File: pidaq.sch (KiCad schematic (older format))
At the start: 42 parts, among them J1 Screw_Terminal_01x08, J2 Screw_Terminal_01x08, J3 Screw_Terminal_01x10, J4 Screw_Terminal_01x10, J5 Conn_01x03_Male, J6 Conn_01x08_Female, U1 LTC2984CLX-DNP, U2 LTC2418IGN-DNP, U3 SN74LV1T34DCKR

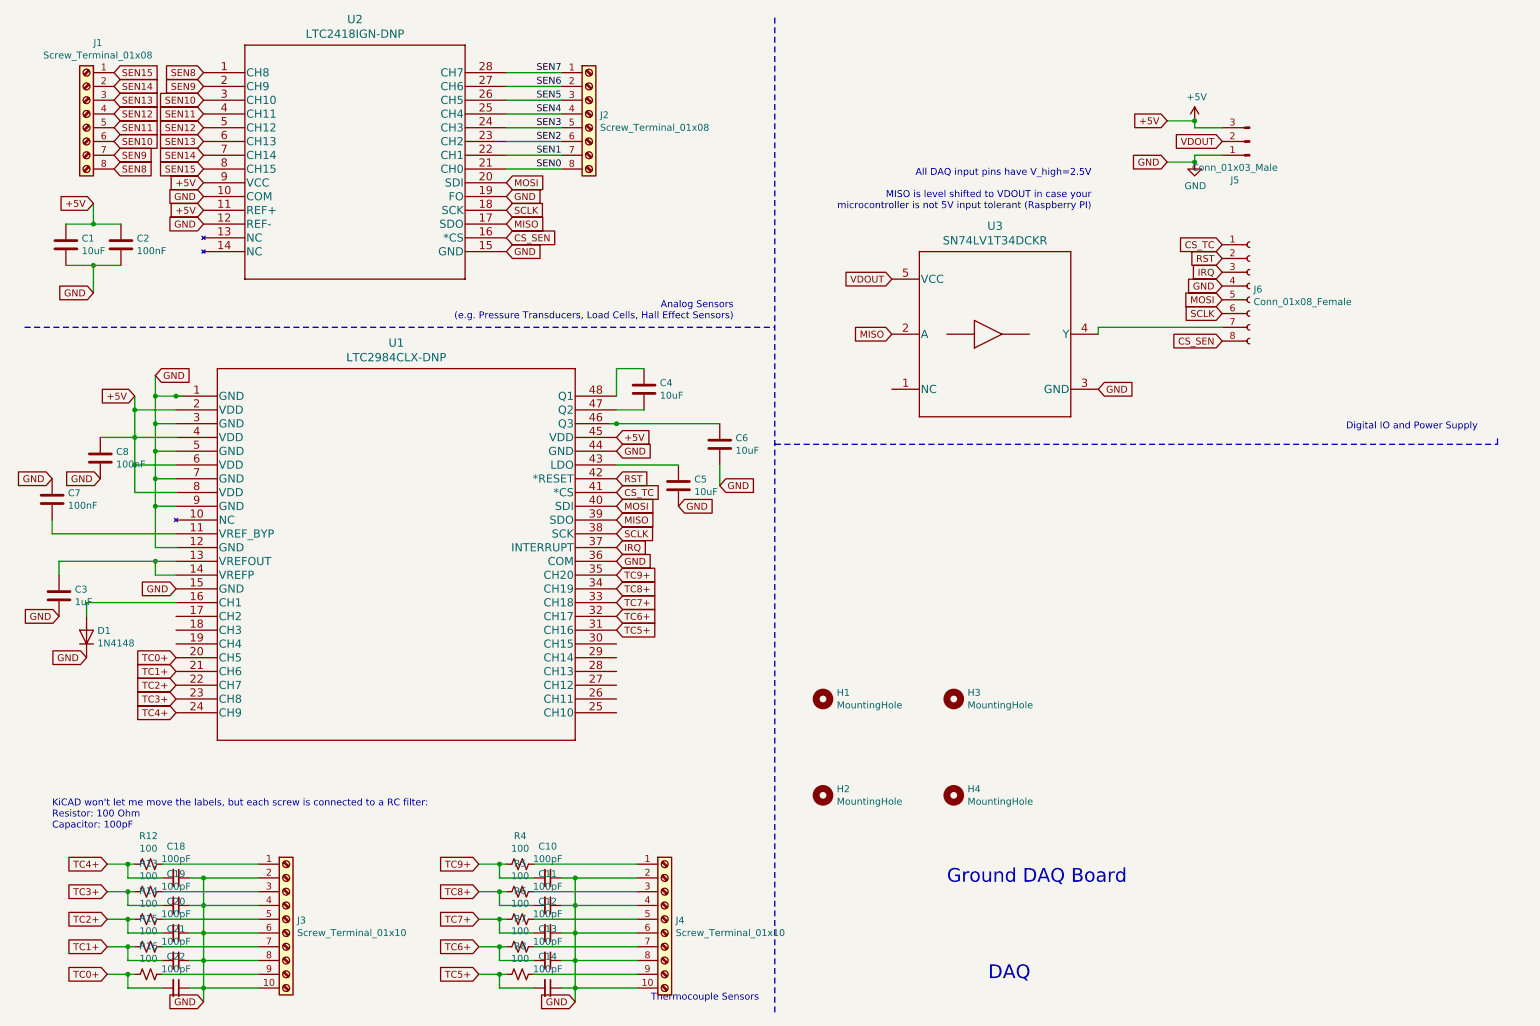
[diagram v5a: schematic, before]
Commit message: reversed screw terminal symbols
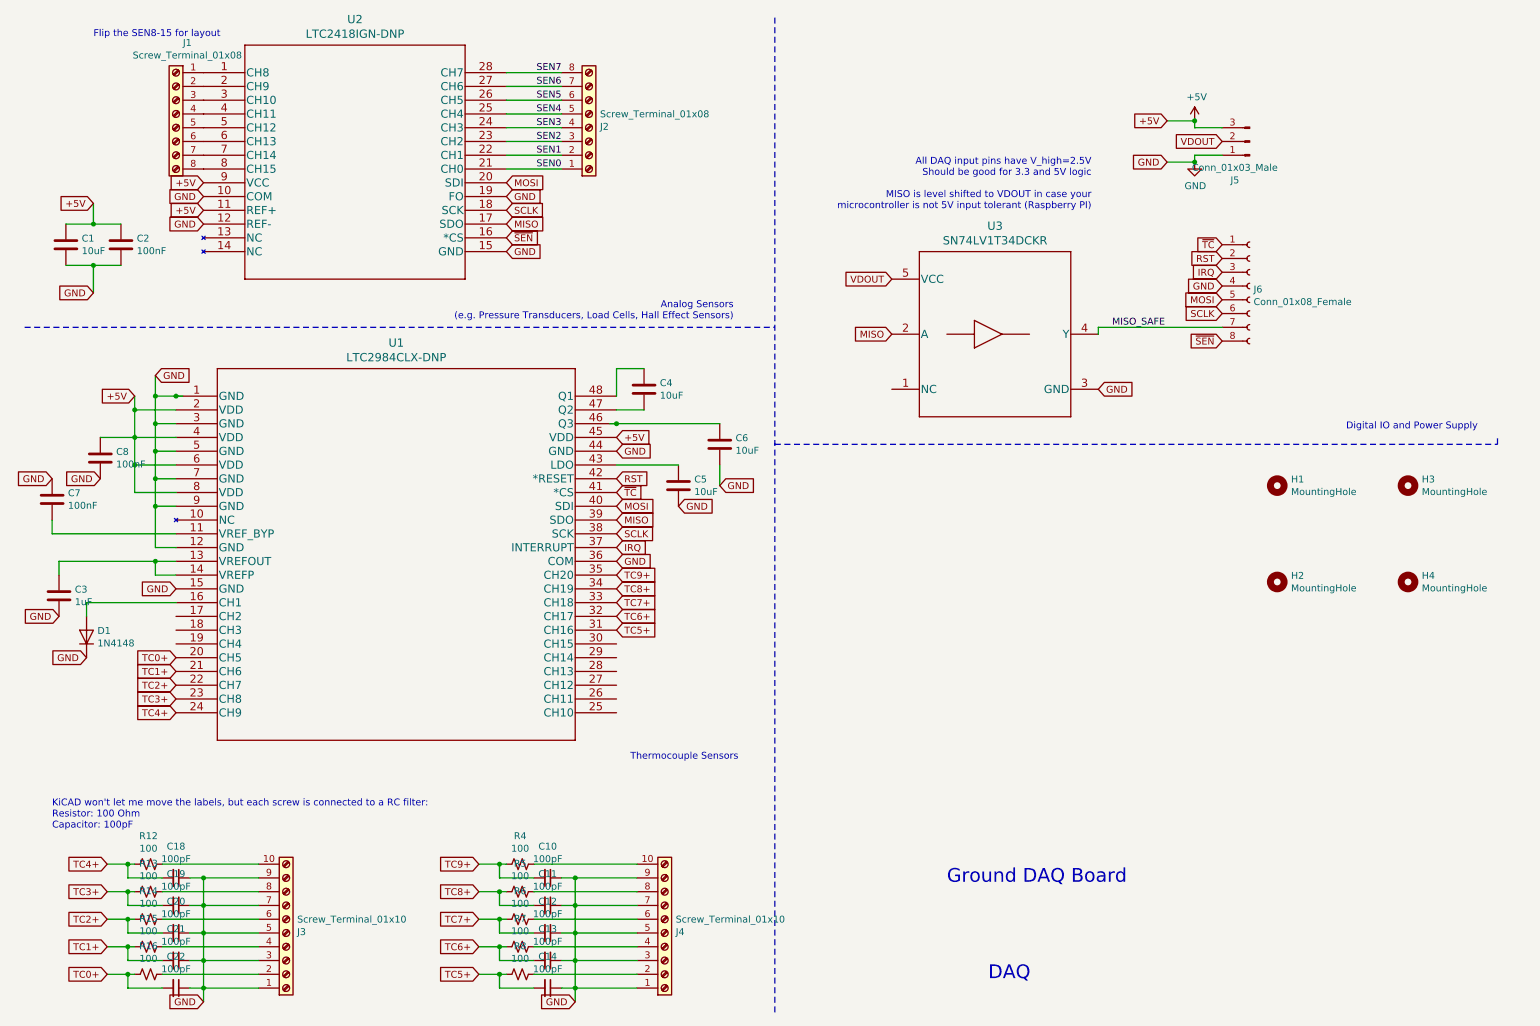
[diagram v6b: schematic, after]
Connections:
- net GND: now also J3.1 (Pin_1), J3.3 (Pin_3), J3.5 (Pin_5), J3.7 (Pin_7), J3.9 (Pin_9), J4.1 (Pin_1), J4.3 (Pin_3), J4.5 (Pin_5), J4.7 (Pin_7), J4.9 (Pin_9); no longer J3.10 (Pin_10), J3.2 (Pin_2), J3.4 (Pin_4), J3.6 (Pin_6), J3.8 (Pin_8), J4.10 (Pin_10), J4.2 (Pin_2), J4.4 (Pin_4), J4.6 (Pin_6), J4.8 (Pin_8)
- net SEN0: now also J2.1 (Pin_1); no longer J2.8 (Pin_8)
- net SEN1: now also J2.2 (Pin_2); no longer J2.7 (Pin_7)
- net SEN2: now also J2.3 (Pin_3); no longer J2.6 (Pin_6)
- net SEN3: now also J2.4 (Pin_4); no longer J2.5 (Pin_5)
- net SEN4: now also J2.5 (Pin_5); no longer J2.4 (Pin_4)
- net SEN5: now also J2.6 (Pin_6); no longer J2.3 (Pin_3)
- net SEN6: now also J2.7 (Pin_7); no longer J2.2 (Pin_2)
- net SEN7: now also J2.8 (Pin_8); no longer J2.1 (Pin_1)
- net MISO_SAFE: now reaches J6.7 (Pin_7), U3.4 (Y)
- net at R4.1: now also J4.10 (Pin_10); no longer J4.1 (Pin_1)
- net at R5.1: now also J4.8 (Pin_8); no longer J4.3 (Pin_3)
- net at R6.1: now also J4.6 (Pin_6); no longer J4.5 (Pin_5)
- net at R7.1: now also J4.4 (Pin_4); no longer J4.7 (Pin_7)
- net at R8.1: now also J4.2 (Pin_2); no longer J4.9 (Pin_9)
- net at R16.1: now also J3.2 (Pin_2); no longer J3.9 (Pin_9)
- net at R15.1: now also J3.4 (Pin_4); no longer J3.7 (Pin_7)
- net at R14.1: now also J3.6 (Pin_6); no longer J3.5 (Pin_5)
- net at R13.1: now also J3.8 (Pin_8); no longer J3.3 (Pin_3)
- net at R12.1: now also J3.10 (Pin_10); no longer J3.1 (Pin_1)
- net CS_SEN renamed ~SEN
- net CS_TC renamed ~TC
- net SEN10: no longer names the net of U2.3 (CH10)
- net SEN10: now also J1.3 (Pin_3); no longer J1.6 (Pin_6)
- net SEN11: no longer names the net of U2.4 (CH11)
- net SEN11: now also J1.4 (Pin_4); no longer J1.5 (Pin_5)
- net SEN12: no longer names the net of U2.5 (CH12)
- net SEN12: now also J1.5 (Pin_5); no longer J1.4 (Pin_4)
- net SEN13: no longer names the net of U2.6 (CH13)
- net SEN13: now also J1.6 (Pin_6); no longer J1.3 (Pin_3)
- net SEN14: no longer names the net of J1.2 (Pin_2)
- net SEN14: now also U2.2 (CH9); no longer U2.7 (CH14)
- net SEN15: no longer names the net of J1.1 (Pin_1)
- net SEN15: now also U2.1 (CH8); no longer U2.8 (CH15)
- net SEN8: no longer names the net of J1.8 (Pin_8)
- net SEN8: now also U2.8 (CH15); no longer U2.1 (CH8)
- net SEN9: no longer names the net of J1.7 (Pin_7)
- net SEN9: now also U2.7 (CH14); no longer U2.2 (CH9)
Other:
- note added: "All DAQ input pins have V_high=2.5V\nShould be good for 3.3 and 5V logic\n\nMISO is level shifted to VDOUT in case your\nmicrocontroller is not 5V input tolerant (Raspberry PI)"
- note added: "Flip the SEN8-15 for layout"
- note removed: "All DAQ input pins have V_high=2.5V\n\nMISO is level shifted to VDOUT in case your\nmicrocontroller is not 5V input tolerant (Raspberry PI)"
- moved on the sheet: H1, H2, H3, H4, J1
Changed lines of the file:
@@
 L Connector:Screw_Terminal_01x08 J2
 U 1 1 5EDBB95D
-P 4550 1250
+P 4550 1350
 AR Path="/5EDBB95D" Ref="J2"  Part="1"
 AR Path="/5ED56214/5EDBB95D" Ref="J?"  Part="1"
-F 0 "J2" H 4630 1242 50  0000 L CNN
-F 1 "Screw_Terminal_01x08" H 4630 1151 50  0000 L CNN
-F 2 "TerminalBlock_Phoenix:TerminalBlock_Phoenix_MKDS-1,5-8-5.08_1x08_P5.08mm_Horizontal" H 4550 1250 50  0001 C CNN
-F 3 "~" H 4550 1250 50  0001 C CNN
-	1    4550 1250
-	1    0    0    -1
+F 0 "J2" H 4630 1342 50  0000 L CNN
+F 1 "Screw_Terminal_01x08" H 4630 1251 50  0000 L CNN
+F 2 "TerminalBlock_Phoenix:TerminalBlock_Phoenix_MKDS-1,5-8-5.08_1x08_P5.08mm_Horizontal" H 4550 1350 50  0001 C CNN
+F 3 "~" H 4550 1350 50  0001 C CNN
+	1    4550 1350
+	1    0    0    1
 $EndComp
 $Comp
 L Connector:Screw_Terminal_01x08 J1
 U 1 1 5EDBB963
-P 900 1250
+P 1550 1250
 AR Path="/5EDBB963" Ref="J1"  Part="1"
 AR Path="/5ED56214/5EDBB963" Ref="J?"  Part="1"
-F 0 "J1" H 818 1767 50  0000 C CNN
-F 1 "Screw_Terminal_01x08" H 818 1676 50  0000 C CNN
-F 2 "TerminalBlock_Phoenix:TerminalBlock_Phoenix_MKDS-1,5-8-5.08_1x08_P5.08mm_Horizontal" H 900 1250 50  0001 C CNN
-F 3 "~" H 900 1250 50  0001 C CNN
-	1    900  1250
+F 0 "J1" H 1468 1767 50  0000 C CNN
+F 1 "Screw_Terminal_01x08" H 1468 1676 50  0000 C CNN
+F 2 "TerminalBlock_Phoenix:TerminalBlock_Phoenix_MKDS-1,5-8-5.08_1x08_P5.08mm_Horizontal" H 1550 1250 50  0001 C CNN
+F 3 "~" H 1550 1250 50  0001 C CNN
+	1    1550 1250
 	-1   0    0    -1
 $EndComp
@@
 SCLK
 Text GLabel 3950 2150 2    50   Input ~ 0
-CS_SEN
+~SEN
 Text Notes 5600 2750 2    50   ~ 0
 Analog Sensors \n(e.g. Pressure Transducers, Load Cells, Hall Effect Sensors)
@@
 RST
 Text GLabel 4750 4000 2    50   Input ~ 0
-CS_TC
+~TC
 Text GLabel 4750 4100 2    50   Input ~ 0
 MOSI
@@
 Wire Wire Line
 	3900 7500 3750 7500
-Text GLabel 1750 950  0    50   Input ~ 0
-SEN8
-Text GLabel 1750 1050 0    50   Input ~ 0
-SEN9
-Text GLabel 1750 1150 0    50   Input ~ 0
-SEN10
-Text GLabel 1750 1250 0    50   Input ~ 0
-SEN11
-Text GLabel 1750 1350 0    50   Input ~ 0
-SEN12
-Text GLabel 1750 1450 0    50   Input ~ 0
-SEN13
-Text GLabel 1750 1550 0    50   Input ~ 0
-SEN14
-Text GLabel 1750 1650 0    50   Input ~ 0
-SEN15
-Text GLabel 1100 950  2    50   Input ~ 0
-SEN15
-Text GLabel 1100 1050 2    50   Input ~ 0
-SEN14
-Text GLabel 1100 1150 2    50   Input ~ 0
-SEN13
-Text GLabel 1100 1250 2    50   Input ~ 0
-SEN12
-Text GLabel 1100 1350 2    50   Input ~ 0
-SEN11
-Text GLabel 1100 1450 2    50   Input ~ 0
-SEN10
-Text GLabel 1100 1550 2    50   Input ~ 0
-SEN9
-Text GLabel 1100 1650 2    50   Input ~ 0
-SEN8
 Text GLabel 4750 4700 2    50   Input ~ 0
 TC8+
@@
 Text GLabel 3750 7100 0    50   Input ~ 0
 TC7+
-Text Notes 5000 7700 0    50   ~ 0
+Text Notes 4850 5950 0    50   ~ 0
 Thermocouple Sensors\n
 $Comp
@@
 $EndComp
 Text GLabel 9150 2900 0    50   Input ~ 0
-CS_SEN
-Text GLabel 9150 2200 0    50   Input ~ 0
-CS_TC
+~SEN
 Text GLabel 9150 2300 0    50   Input ~ 0
 RST
@@
 L Connector:Screw_Terminal_01x10 J3
 U 1 1 5F0EBDBF
-P 2350 7100
-F 0 "J3" H 2430 7092 50  0000 L CNN
-F 1 "Screw_Terminal_01x10" H 2430 7001 50  0000 L CNN
-F 2 "TerminalBlock_Phoenix:TerminalBlock_Phoenix_PT-1,5-10-3.5-H_1x10_P3.50mm_Horizontal" H 2350 7100 50  0001 C CNN
-F 3 "~" H 2350 7100 50  0001 C CNN
-	1    2350 7100
-	1    0    0    -1
-$EndComp
-$Comp
-L Connector:Screw_Terminal_01x10 J4
-U 1 1 5F0EED09
-P 5100 7100
-F 0 "J4" H 5180 7092 50  0000 L CNN
-F 1 "Screw_Terminal_01x10" H 5180 7001 50  0000 L CNN
-F 2 "TerminalBlock_Phoenix:TerminalBlock_Phoenix_PT-1,5-10-3.5-H_1x10_P3.50mm_Horizontal" H 5100 7100 50  0001 C CNN
-F 3 "~" H 5100 7100 50  0001 C CNN
-	1    5100 7100
-	1    0    0    -1
+P 2350 7200
+F 0 "J3" H 2430 7192 50  0000 L CNN
+F 1 "Screw_Terminal_01x10" H 2430 7101 50  0000 L CNN
+F 2 "TerminalBlock_Phoenix:TerminalBlock_Phoenix_PT-1,5-10-3.5-H_1x10_P3.50mm_Horizontal" H 2350 7200 50  0001 C CNN
+F 3 "~" H 2350 7200 50  0001 C CNN
+	1    2350 7200
+	1    0    0    1
 $EndComp
 Wire Wire Line
@@
 	1450 6700 2150 6700
 Wire Wire Line
-	4150 6700 4900 6700
-Wire Wire Line
-	4450 6800 4900 6800
-Wire Wire Line
-	4150 6900 4900 6900
-Wire Wire Line
 	4350 7000 4450 7000
-Wire Wire Line
-	4450 7000 4900 7000
-Wire Wire Line
-	4150 7100 4900 7100
-Wire Wire Line
-	4450 7200 4900 7200
-Wire Wire Line
-	4150 7300 4900 7300
-Wire Wire Line
-	4450 7400 4900 7400
-Wire Wire Line
-	4150 7500 4900 7500
-Wire Wire Line
-	4450 7600 4900 7600
 $Comp
 L Diode:1N4148 D1
@@
 L Mechanical:MountingHole H1
 U 1 1 5ED3CDC2
-P 6250 5500
-F 0 "H1" H 6350 5546 50  0000 L CNN
-F 1 "MountingHole" H 6350 5455 50  0000 L CNN
-F 2 "MountingHole:MountingHole_3.2mm_M3" H 6250 5500 50  0001 C CNN
-F 3 "~" H 6250 5500 50  0001 C CNN
-	1    6250 5500
+P 9550 3950
+F 0 "H1" H 9650 3996 50  0000 L CNN
+F 1 "MountingHole" H 9650 3905 50  0000 L CNN
+F 2 "MountingHole:MountingHole_3.2mm_M3" H 9550 3950 50  0001 C CNN
+F 3 "~" H 9550 3950 50  0001 C CNN
+	1    9550 3950
 	1    0    0    -1
 $EndComp
@@
 L Mechanical:MountingHole H3
 U 1 1 5ED3DEFD
-P 7200 5500
-F 0 "H3" H 7300 5546 50  0000 L CNN
-F 1 "MountingHole" H 7300 5455 50  0000 L CNN
-F 2 "MountingHole:MountingHole_3.2mm_M3" H 7200 5500 50  0001 C CNN
-F 3 "~" H 7200 5500 50  0001 C CNN
-	1    7200 5500
+P 10500 3950
+F 0 "H3" H 10600 3996 50  0000 L CNN
+F 1 "MountingHole" H 10600 3905 50  0000 L CNN
+F 2 "MountingHole:MountingHole_3.2mm_M3" H 10500 3950 50  0001 C CNN
+F 3 "~" H 10500 3950 50  0001 C CNN
+	1    10500 3950
 	1    0    0    -1
 $EndComp
@@
 L Mechanical:MountingHole H2
 U 1 1 5ED3EC92
-P 6250 6200
-F 0 "H2" H 6350 6246 50  0000 L CNN
-F 1 "MountingHole" H 6350 6155 50  0000 L CNN
-F 2 "MountingHole:MountingHole_3.2mm_M3" H 6250 6200 50  0001 C CNN
-F 3 "~" H 6250 6200 50  0001 C CNN
-	1    6250 6200
+P 9550 4650
+F 0 "H2" H 9650 4696 50  0000 L CNN
+F 1 "MountingHole" H 9650 4605 50  0000 L CNN
+F 2 "MountingHole:MountingHole_3.2mm_M3" H 9550 4650 50  0001 C CNN
+F 3 "~" H 9550 4650 50  0001 C CNN
+	1    9550 4650
 	1    0    0    -1
 $EndComp
@@
 L Mechanical:MountingHole H4
 U 1 1 5ED3F653
-P 7200 6200
-F 0 "H4" H 7300 6246 50  0000 L CNN
-F 1 "MountingHole" H 7300 6155 50  0000 L CNN
-F 2 "MountingHole:MountingHole_3.2mm_M3" H 7200 6200 50  0001 C CNN
-F 3 "~" H 7200 6200 50  0001 C CNN
-	1    7200 6200
+P 10500 4650
+F 0 "H4" H 10600 4696 50  0000 L CNN
+F 1 "MountingHole" H 10600 4605 50  0000 L CNN
+F 2 "MountingHole:MountingHole_3.2mm_M3" H 10500 4650 50  0001 C CNN
+F 3 "~" H 10500 4650 50  0001 C CNN
+	1    10500 4650
 	1    0    0    -1
 $EndComp
@@
 Digital IO and Power Supply
 Text Notes 8200 1950 2    50   ~ 0
-All DAQ input pins have V_high=2.5V\n\nMISO is level shifted to VDOUT in case your\nmicrocontroller is not 5V input tolerant (Raspberry PI)
+All DAQ input pins have V_high=2.5V\nShould be good for 3.3 and 5V logic\n\nMISO is level shifted to VDOUT in case your\nmicrocontroller is not 5V input tolerant (Raspberry PI)
+Text Label 8350 2800 0    50   ~ 0
+MISO_SAFE
+Text Notes 950  700  0    50   ~ 0
+Flip the SEN8-15 for layout
+Text GLabel 9150 2200 0    50   Input ~ 0
+~TC
+Wire Wire Line
+	4450 7600 4900 7600
+Wire Wire Line
+	4150 7500 4900 7500
+Wire Wire Line
+	4450 7400 4900 7400
+Wire Wire Line
+	4150 7300 4900 7300
+Wire Wire Line
+	4450 7200 4900 7200
+Wire Wire Line
+	4150 7100 4900 7100
+Wire Wire Line
+	4450 7000 4900 7000
+Wire Wire Line
+	4150 6900 4900 6900
+Wire Wire Line
+	4450 6800 4900 6800
+Wire Wire Line
+	4150 6700 4900 6700
+$Comp
+L Connector:Screw_Terminal_01x10 J4
+U 1 1 5F0EED09
+P 5100 7200
+F 0 "J4" H 5180 7192 50  0000 L CNN
+F 1 "Screw_Terminal_01x10" H 5180 7101 50  0000 L CNN
+F 2 "TerminalBlock_Phoenix:TerminalBlock_Phoenix_PT-1,5-10-3.5-H_1x10_P3.50mm_Horizontal" H 5100 7200 50  0001 C CNN
+F 3 "~" H 5100 7200 50  0001 C CNN
+	1    5100 7200
+	1    0    0    1
+$EndComp
 $EndSCHEMATC

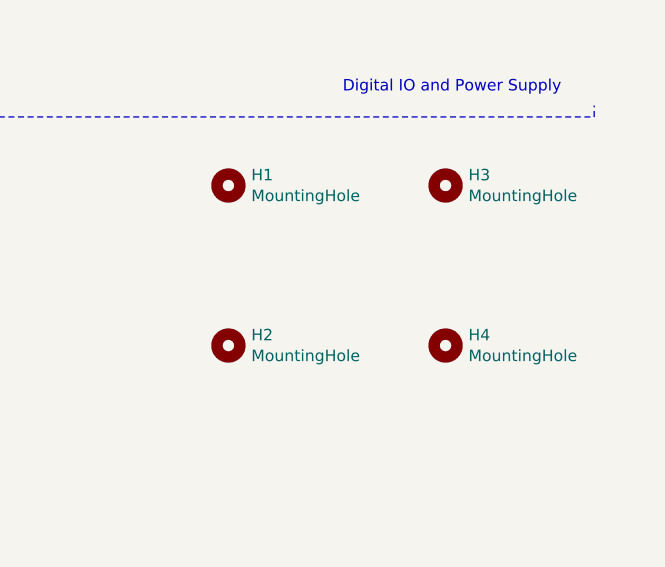
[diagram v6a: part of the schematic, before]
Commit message: turn screw holes into plated ones for more grounding
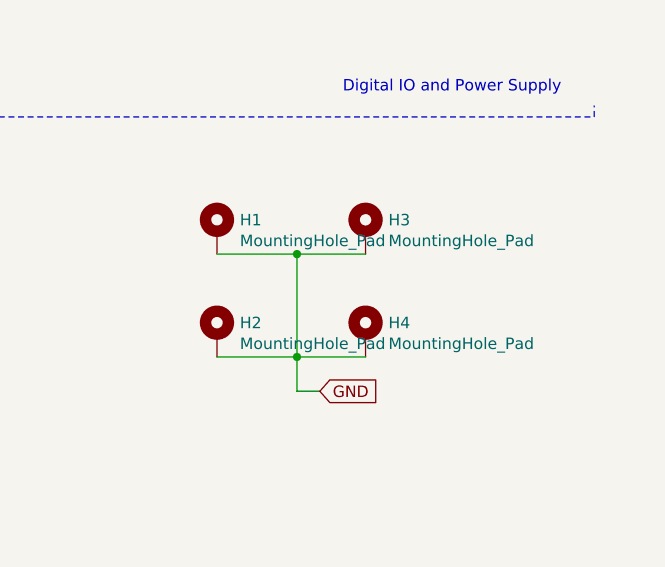
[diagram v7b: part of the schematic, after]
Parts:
- removed H1, H2, H3, H4: MountingHole, MountingHole:MountingHole_3.2mm_M3, symbol Mechanical:MountingHole
- added H1, H2, H3, H4: MountingHole_Pad, MountingHole:MountingHole_3.2mm_M3_Pad_Via, symbol Mechanical:MountingHole_Pad
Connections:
- net GND: now also H1.1, H2.1, H3.1, H4.1
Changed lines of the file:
@@
 	0    -1   -1   0
-$EndComp
-$Comp
-L Mechanical:MountingHole H1
-U 1 1 5ED3CDC2
-P 9550 3950
-F 0 "H1" H 9650 3996 50  0000 L CNN
-F 1 "MountingHole" H 9650 3905 50  0000 L CNN
-F 2 "MountingHole:MountingHole_3.2mm_M3" H 9550 3950 50  0001 C CNN
-F 3 "~" H 9550 3950 50  0001 C CNN
-	1    9550 3950
-	1    0    0    -1
-$EndComp
-$Comp
-L Mechanical:MountingHole H3
-U 1 1 5ED3DEFD
-P 10500 3950
-F 0 "H3" H 10600 3996 50  0000 L CNN
-F 1 "MountingHole" H 10600 3905 50  0000 L CNN
-F 2 "MountingHole:MountingHole_3.2mm_M3" H 10500 3950 50  0001 C CNN
-F 3 "~" H 10500 3950 50  0001 C CNN
-	1    10500 3950
-	1    0    0    -1
-$EndComp
-$Comp
-L Mechanical:MountingHole H2
-U 1 1 5ED3EC92
-P 9550 4650
-F 0 "H2" H 9650 4696 50  0000 L CNN
-F 1 "MountingHole" H 9650 4605 50  0000 L CNN
-F 2 "MountingHole:MountingHole_3.2mm_M3" H 9550 4650 50  0001 C CNN
-F 3 "~" H 9550 4650 50  0001 C CNN
-	1    9550 4650
-	1    0    0    -1
-$EndComp
-$Comp
-L Mechanical:MountingHole H4
-U 1 1 5ED3F653
-P 10500 4650
-F 0 "H4" H 10600 4696 50  0000 L CNN
-F 1 "MountingHole" H 10600 4605 50  0000 L CNN
-F 2 "MountingHole:MountingHole_3.2mm_M3" H 10500 4650 50  0001 C CNN
-F 3 "~" H 10500 4650 50  0001 C CNN
-	1    10500 4650
-	1    0    0    -1
 $EndComp
 Text Notes 650  6450 0    50   ~ 0
@@
 	1    0    0    1
 $EndComp
+$Comp
+L Mechanical:MountingHole_Pad H1
+U 1 1 5EDC0B75
+P 9500 4150
+F 0 "H1" H 9600 4199 50  0000 L CNN
+F 1 "MountingHole_Pad" H 9600 4108 50  0000 L CNN
+F 2 "MountingHole:MountingHole_3.2mm_M3_Pad_Via" H 9500 4150 50  0001 C CNN
+F 3 "~" H 9500 4150 50  0001 C CNN
+	1    9500 4150
+	1    0    0    -1
+$EndComp
+$Comp
+L Mechanical:MountingHole_Pad H3
+U 1 1 5EDC14E8
+P 10150 4150
+F 0 "H3" H 10250 4199 50  0000 L CNN
+F 1 "MountingHole_Pad" H 10250 4108 50  0000 L CNN
+F 2 "MountingHole:MountingHole_3.2mm_M3_Pad_Via" H 10150 4150 50  0001 C CNN
+F 3 "~" H 10150 4150 50  0001 C CNN
+	1    10150 4150
+	1    0    0    -1
+$EndComp
+$Comp
+L Mechanical:MountingHole_Pad H2
+U 1 1 5EDC1970
+P 9500 4600
+F 0 "H2" H 9600 4649 50  0000 L CNN
+F 1 "MountingHole_Pad" H 9600 4558 50  0000 L CNN
+F 2 "MountingHole:MountingHole_3.2mm_M3_Pad_Via" H 9500 4600 50  0001 C CNN
+F 3 "~" H 9500 4600 50  0001 C CNN
+	1    9500 4600
+	1    0    0    -1
+$EndComp
+$Comp
+L Mechanical:MountingHole_Pad H4
+U 1 1 5EDC2A10
+P 10150 4600
+F 0 "H4" H 10250 4649 50  0000 L CNN
+F 1 "MountingHole_Pad" H 10250 4558 50  0000 L CNN
+F 2 "MountingHole:MountingHole_3.2mm_M3_Pad_Via" H 10150 4600 50  0001 C CNN
+F 3 "~" H 10150 4600 50  0001 C CNN
+	1    10150 4600
+	1    0    0    -1
+$EndComp
+Wire Wire Line
+	9500 4250 9850 4250
+Wire Wire Line
+	9850 4250 9850 4700
+Wire Wire Line
+	9850 4700 9500 4700
+Connection ~ 9850 4250
+Wire Wire Line
+	9850 4250 10150 4250
+Wire Wire Line
+	9850 4700 10150 4700
+Connection ~ 9850 4700
+Wire Wire Line
+	9850 4700 9850 4850
+Wire Wire Line
+	9850 4850 9950 4850
+Text GLabel 9950 4850 2    50   Input ~ 0
+GND
 $EndSCHEMATC
